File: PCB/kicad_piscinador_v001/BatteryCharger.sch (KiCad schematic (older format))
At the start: 0 parts

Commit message: PCB ----------------- Update
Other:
- note added: "Battery charger"
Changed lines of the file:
@@
 Comment4 ""
 $EndDescr
+Text Notes 3050 1800 0    60   ~ 12
+Battery charger
 $EndSCHEMATC

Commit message: project backup
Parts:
- added BAT?: BATTERY, symbol BATTERY
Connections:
- new net V_gnd: BAT?.2 (-)
- new net V_motor: BAT?.1 (+)
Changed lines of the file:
@@
 LIBS:Zilog
 LIBS:Common-Parts-Library
+LIBS:freetronics_schematic
 LIBS:kicad_test_picinador-cache
 EELAYER 25 0
@@
 Text Notes 3050 1800 0    60   ~ 12
 Battery charger
+$Comp
+L BATTERY BAT?
+U 1 1 57FFC7C9
+P 3400 3000
+F 0 "BAT?" H 3400 3200 50  0000 C CNN
+F 1 "BATTERY" H 3400 2810 50  0000 C CNN
+F 2 "" H 3400 3000 60  0000 C CNN
+F 3 "" H 3400 3000 60  0000 C CNN
+	1    3400 3000
+	0    1    1    0
+$EndComp
+Text HLabel 5000 2700 2    60   Output ~ 0
+V_motor
+Text HLabel 5000 3300 2    60   Output ~ 0
+V_gnd
+Wire Wire Line
+	5000 3300 3400 3300
+Wire Wire Line
+	3400 2700 5000 2700
 $EndSCHEMATC

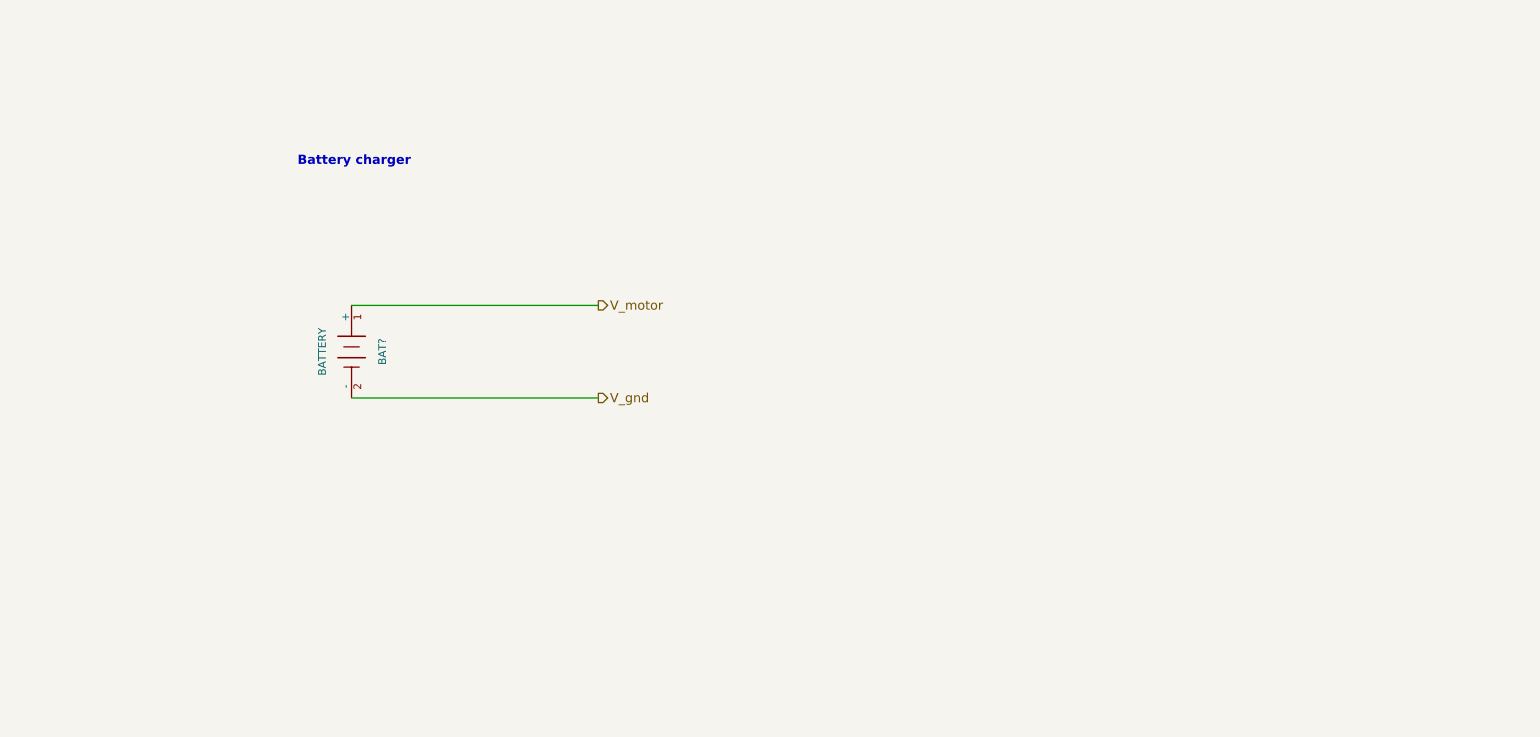
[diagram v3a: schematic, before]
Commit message: Piscinador----------------- Add ltc3121 boost converter
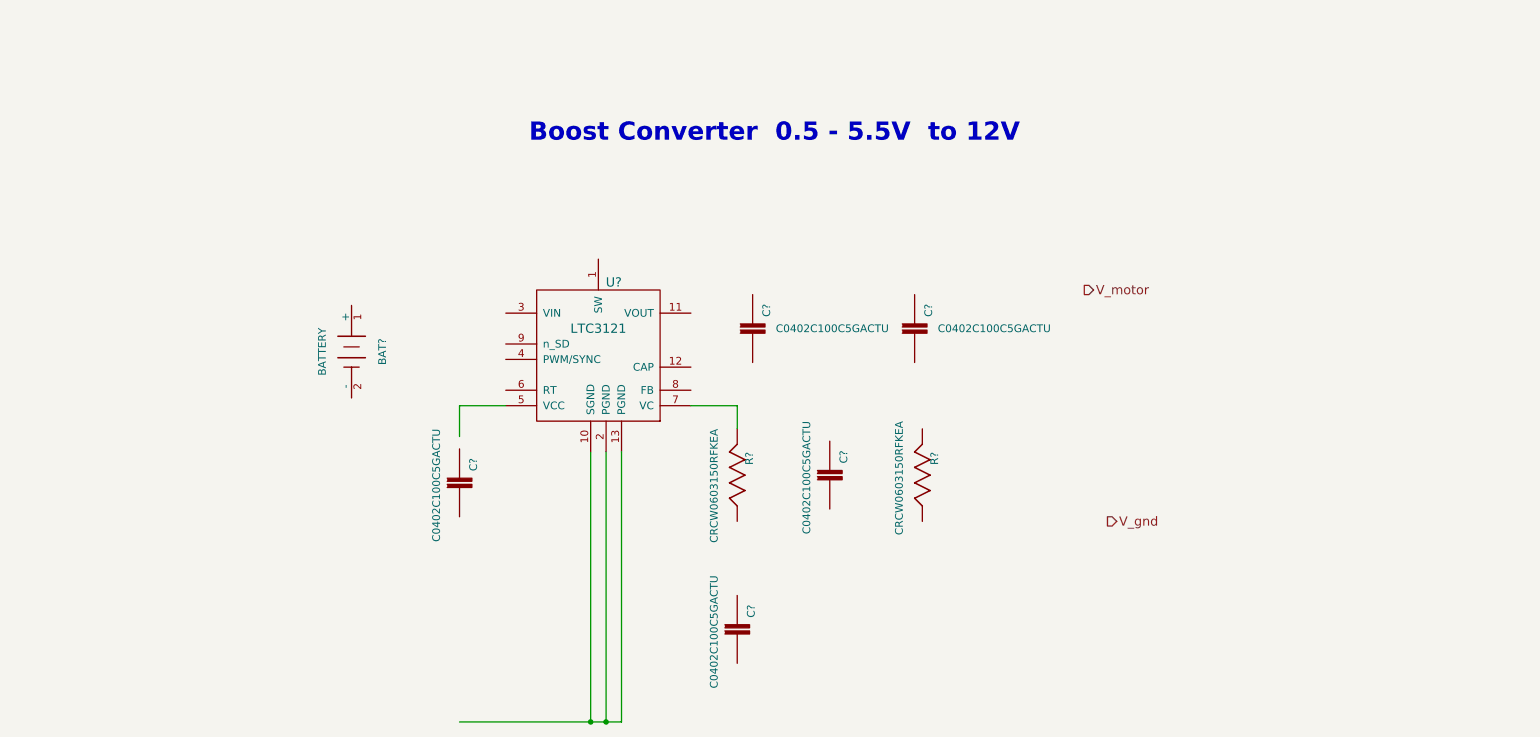
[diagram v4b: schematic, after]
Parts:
- added C? (x5): C0402C100C5GACTU, C0402C100C5GACTU_CAPC1005X60, symbol C0402C100C5GACTU
- added R? (x2): CRCW0603150RFKEA, CRCW0603150RFKEA_RESC1608X55, symbol CRCW0603150RFKEA
- added U?: LTC3121, 12-Lead (4mm × 3mm) Plastic DFN, symbol LTC3121
- BAT?: Manufacturer (none) -> Samsumg
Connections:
- wire segments 2 -> 8
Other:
- note added: "Boost Converter 0.5 - 5.5V to 12V"
- note removed: "Battery charger"
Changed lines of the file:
@@
 LIBS:Zilog
 LIBS:Common-Parts-Library
-LIBS:freetronics_schematic
 LIBS:kicad_test_picinador-cache
 EELAYER 25 0
@@
 encoding utf-8
 Sheet 2 2
-Title "Battery Chager"
-Date ""
+Title "System Spannug "
+Date "2016-10-15"
 Rev ""
-Comp ""
+Comp "JVC-Home"
 Comment1 ""
 Comment2 ""
@@
 Comment4 ""
 $EndDescr
-Text Notes 3050 1800 0    60   ~ 12
-Battery charger
+Text Notes 4550 1650 0    118  ~ 24
+Boost Converter  0.5 - 5.5V  to 12V
 $Comp
 L BATTERY BAT?
@@
 F 2 "" H 3400 3000 60  0000 C CNN
 F 3 "" H 3400 3000 60  0000 C CNN
+F 4 "Samsumg" H 3400 3000 60  0001 C CNN "Manufacturer"
 	1    3400 3000
 	0    1    1    0
 $EndComp
-Text HLabel 5000 2700 2    60   Output ~ 0
+Text HLabel 8150 2600 2    60   Output ~ 0
 V_motor
-Text HLabel 5000 3300 2    60   Output ~ 0
+Text HLabel 8300 4100 2    60   Output ~ 0
 V_gnd
+$Comp
+L LTC3121 U?
+U 1 1 58028389
+P 5050 3150
+F 0 "U?" H 5100 3750 60  0000 C CNN
+F 1 "LTC3121" H 5000 3450 60  0000 C CNN
+F 2 "12-Lead (4mm × 3mm) Plastic DFN" H 5050 3150 60  0001 C CNN
+F 3 "" H 5050 3150 60  0001 C CNN
+F 4 "Linear" H 5050 3150 60  0001 C CNN "Manufaturer"
+F 5 "LTC3121EDE#PBF" H 5050 3150 60  0001 C CNN "Manufacurer No"
+	1    5050 3150
+	1    0    0    -1
+$EndComp
+$Comp
+L C0402C100C5GACTU C?
+U 1 1 580286AA
+P 6000 2850
+F 0 "C?" H 5840 2940 50  0000 L CNN
+F 1 "C0402C100C5GACTU" V 6000 3000 50  0000 L CNN
+F 2 "C0402C100C5GACTU_CAPC1005X60" H 6000 2850 50  0001 L CNN
+F 3 "KEMET" H 6000 2850 50  0001 L CNN
+	1    6000 2850
+	0    1    1    0
+$EndComp
+$Comp
+L CRCW0603150RFKEA R?
+U 1 1 58028919
+P 5900 3800
+F 0 "R?" H 5750 3879 50  0000 L CNN
+F 1 "CRCW0603150RFKEA" H 5600 3650 50  0000 L CNN
+F 2 "CRCW0603150RFKEA_RESC1608X55" H 5900 3800 50  0001 L CNN
+F 3 "VISHAY" H 5900 3800 50  0001 L CNN
+	1    5900 3800
+	0    1    1    0
+$EndComp
+$Comp
+L CRCW0603150RFKEA R?
+U 1 1 58028B0E
+P 7100 3800
+F 0 "R?" H 6950 3879 50  0000 L CNN
+F 1 "CRCW0603150RFKEA" H 6750 3650 50  0000 L CNN
+F 2 "CRCW0603150RFKEA_RESC1608X55" H 7100 3800 50  0001 L CNN
+F 3 "VISHAY" H 7100 3800 50  0001 L CNN
+	1    7100 3800
+	0    1    1    0
+$EndComp
+$Comp
+L C0402C100C5GACTU C?
+U 1 1 58028B45
+P 6500 3800
+F 0 "C?" H 6340 3890 50  0000 L CNN
+F 1 "C0402C100C5GACTU" H 6150 3650 50  0000 L CNN
+F 2 "C0402C100C5GACTU_CAPC1005X60" H 6500 3800 50  0001 L CNN
+F 3 "KEMET" H 6500 3800 50  0001 L CNN
+	1    6500 3800
+	0    1    1    0
+$EndComp
+$Comp
+L C0402C100C5GACTU C?
+U 1 1 58028B7D
+P 7050 2850
+F 0 "C?" H 6890 2940 50  0000 L CNN
+F 1 "C0402C100C5GACTU" V 7050 3000 50  0000 L CNN
+F 2 "C0402C100C5GACTU_CAPC1005X60" H 7050 2850 50  0001 L CNN
+F 3 "KEMET" H 7050 2850 50  0001 L CNN
+	1    7050 2850
+	0    1    1    0
+$EndComp
+$Comp
+L C0402C100C5GACTU C?
+U 1 1 5802911A
+P 4100 3850
+F 0 "C?" H 3940 3940 50  0000 L CNN
+F 1 "C0402C100C5GACTU" H 3750 3700 50  0000 L CNN
+F 2 "C0402C100C5GACTU_CAPC1005X60" H 4100 3850 50  0001 L CNN
+F 3 "KEMET" H 4100 3850 50  0001 L CNN
+	1    4100 3850
+	0    1    1    0
+$EndComp
 Wire Wire Line
-	5000 3300 3400 3300
+	4100 3550 4100 3350
 Wire Wire Line
-	3400 2700 5000 2700
+	4100 3350 4400 3350
+Wire Wire Line
+	4950 3650 4950 5400
+Wire Wire Line
+	5150 5400 4100 5400
+Wire Wire Line
+	5050 3650 5050 5400
+Wire Wire Line
+	5150 3650 5150 5400
+Connection ~ 5050 5400
+Connection ~ 4950 5400
+$Comp
+L C0402C100C5GACTU C?
+U 1 1 5802B8AF
+P 5900 4800
+F 0 "C?" H 5740 4890 50  0000 L CNN
+F 1 "C0402C100C5GACTU" H 5550 4650 50  0000 L CNN
+F 2 "C0402C100C5GACTU_CAPC1005X60" H 5900 4800 50  0001 L CNN
+F 3 "KEMET" H 5900 4800 50  0001 L CNN
+	1    5900 4800
+	0    1    1    0
+$EndComp
+Wire Wire Line
+	5600 3350 5900 3350
+Wire Wire Line
+	5900 3350 5900 3500
 $EndSCHEMATC

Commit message: add plug to charge the battery
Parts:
- removed C? (x5): C0402C100C5GACTU, C0402C100C5GACTU_CAPC1005X60, symbol C0402C100C5GACTU
- added C? (x3): C, symbol C
- added P?: CON_JACK_MONO_SW, symbol CON_JACK_MONO_SW
- added R?: CRCW0603150RFKEA, CRCW0603150RFKEA_RESC1608X55, symbol CRCW0603150RFKEA
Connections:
- wire segments 8 -> 30
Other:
- note added: "Energy harvesting and battery charger"
- moved on the sheet: BAT?, R?, U?
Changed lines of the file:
@@
 LIBS:Zilog
 LIBS:Common-Parts-Library
+LIBS:freetronics_schematic
 LIBS:kicad_test_picinador-cache
 EELAYER 25 0
@@
 Comment4 ""
 $EndDescr
-Text Notes 4550 1650 0    118  ~ 24
+Text Notes 6100 1100 0    118  ~ 24
 Boost Converter  0.5 - 5.5V  to 12V
 $Comp
 L BATTERY BAT?
 U 1 1 57FFC7C9
-P 3400 3000
-F 0 "BAT?" H 3400 3200 50  0000 C CNN
-F 1 "BATTERY" H 3400 2810 50  0000 C CNN
-F 2 "" H 3400 3000 60  0000 C CNN
-F 3 "" H 3400 3000 60  0000 C CNN
-F 4 "Samsumg" H 3400 3000 60  0001 C CNN "Manufacturer"
-	1    3400 3000
+P 6350 3150
+F 0 "BAT?" H 6350 3350 50  0000 C CNN
+F 1 "BATTERY" H 6350 2960 50  0000 C CNN
+F 2 "" H 6350 3150 60  0000 C CNN
+F 3 "" H 6350 3150 60  0000 C CNN
+F 4 "Samsumg" H 6350 3150 60  0001 C CNN "Manufacturer"
+	1    6350 3150
 	0    1    1    0
 $EndComp
-Text HLabel 8150 2600 2    60   Output ~ 0
+Text HLabel 10500 2550 2    60   Output ~ 0
 V_motor
-Text HLabel 8300 4100 2    60   Output ~ 0
+Text HLabel 10600 4650 2    60   Output ~ 0
 V_gnd
 $Comp
 L LTC3121 U?
 U 1 1 58028389
-P 5050 3150
-F 0 "U?" H 5100 3750 60  0000 C CNN
-F 1 "LTC3121" H 5000 3450 60  0000 C CNN
-F 2 "12-Lead (4mm × 3mm) Plastic DFN" H 5050 3150 60  0001 C CNN
-F 3 "" H 5050 3150 60  0001 C CNN
-F 4 "Linear" H 5050 3150 60  0001 C CNN "Manufaturer"
-F 5 "LTC3121EDE#PBF" H 5050 3150 60  0001 C CNN "Manufacurer No"
-	1    5050 3150
+P 8000 3100
+F 0 "U?" H 8050 3700 60  0000 C CNN
+F 1 "LTC3121" H 7950 3400 60  0000 C CNN
+F 2 "12-Lead (4mm × 3mm) Plastic DFN" H 8000 3100 60  0001 C CNN
+F 3 "" H 8000 3100 60  0001 C CNN
+F 4 "Linear" H 8000 3100 60  0001 C CNN "Manufaturer"
+F 5 "LTC3121EDE#PBF" H 8000 3100 60  0001 C CNN "Manufacurer No"
+	1    8000 3100
 	1    0    0    -1
-$EndComp
-$Comp
-L C0402C100C5GACTU C?
-U 1 1 580286AA
-P 6000 2850
-F 0 "C?" H 5840 2940 50  0000 L CNN
-F 1 "C0402C100C5GACTU" V 6000 3000 50  0000 L CNN
-F 2 "C0402C100C5GACTU_CAPC1005X60" H 6000 2850 50  0001 L CNN
-F 3 "KEMET" H 6000 2850 50  0001 L CNN
-	1    6000 2850
-	0    1    1    0
 $EndComp
 $Comp
 L CRCW0603150RFKEA R?
 U 1 1 58028919
-P 5900 3800
-F 0 "R?" H 5750 3879 50  0000 L CNN
-F 1 "CRCW0603150RFKEA" H 5600 3650 50  0000 L CNN
-F 2 "CRCW0603150RFKEA_RESC1608X55" H 5900 3800 50  0001 L CNN
-F 3 "VISHAY" H 5900 3800 50  0001 L CNN
-	1    5900 3800
+P 8850 3750
+F 0 "R?" H 8700 3829 50  0000 L CNN
+F 1 "CRCW0603150RFKEA" H 8550 3600 50  0000 L CNN
+F 2 "CRCW0603150RFKEA_RESC1608X55" H 8850 3750 50  0001 L CNN
+F 3 "VISHAY" H 8850 3750 50  0001 L CNN
+	1    8850 3750
 	0    1    1    0
 $EndComp
@@
 L CRCW0603150RFKEA R?
 U 1 1 58028B0E
-P 7100 3800
-F 0 "R?" H 6950 3879 50  0000 L CNN
-F 1 "CRCW0603150RFKEA" H 6750 3650 50  0000 L CNN
-F 2 "CRCW0603150RFKEA_RESC1608X55" H 7100 3800 50  0001 L CNN
-F 3 "VISHAY" H 7100 3800 50  0001 L CNN
-	1    7100 3800
-	0    1    1    0
-$EndComp
-$Comp
-L C0402C100C5GACTU C?
-U 1 1 58028B45
-P 6500 3800
-F 0 "C?" H 6340 3890 50  0000 L CNN
-F 1 "C0402C100C5GACTU" H 6150 3650 50  0000 L CNN
-F 2 "C0402C100C5GACTU_CAPC1005X60" H 6500 3800 50  0001 L CNN
-F 3 "KEMET" H 6500 3800 50  0001 L CNN
-	1    6500 3800
-	0    1    1    0
-$EndComp
-$Comp
-L C0402C100C5GACTU C?
-U 1 1 58028B7D
-P 7050 2850
-F 0 "C?" H 6890 2940 50  0000 L CNN
-F 1 "C0402C100C5GACTU" V 7050 3000 50  0000 L CNN
-F 2 "C0402C100C5GACTU_CAPC1005X60" H 7050 2850 50  0001 L CNN
-F 3 "KEMET" H 7050 2850 50  0001 L CNN
-	1    7050 2850
-	0    1    1    0
-$EndComp
-$Comp
-L C0402C100C5GACTU C?
-U 1 1 5802911A
-P 4100 3850
-F 0 "C?" H 3940 3940 50  0000 L CNN
-F 1 "C0402C100C5GACTU" H 3750 3700 50  0000 L CNN
-F 2 "C0402C100C5GACTU_CAPC1005X60" H 4100 3850 50  0001 L CNN
-F 3 "KEMET" H 4100 3850 50  0001 L CNN
-	1    4100 3850
+P 9350 3750
+F 0 "R?" H 9200 3829 50  0000 L CNN
+F 1 "CRCW0603150RFKEA" H 9000 3600 50  0000 L CNN
+F 2 "CRCW0603150RFKEA_RESC1608X55" H 9350 3750 50  0001 L CNN
+F 3 "VISHAY" H 9350 3750 50  0001 L CNN
+	1    9350 3750
 	0    1    1    0
 $EndComp
 Wire Wire Line
-	4100 3550 4100 3350
+	7200 3300 7200 3650
 Wire Wire Line
-	4100 3350 4400 3350
+	7200 3300 7500 3300
 Wire Wire Line
-	4950 3650 4950 5400
+	7900 3600 7900 4650
 Wire Wire Line
-	5150 5400 4100 5400
+	5600 4650 6350 4650
 Wire Wire Line
-	5050 3650 5050 5400
+	6350 4650 7200 4650
 Wire Wire Line
-	5150 3650 5150 5400
-Connection ~ 5050 5400
-Connection ~ 4950 5400
+	7200 4650 7900 4650
+Wire Wire Line
+	7900 4650 8000 4650
+Wire Wire Line
+	8000 4650 8100 4650
+Wire Wire Line
+	8100 4650 8850 4650
+Wire Wire Line
+	8850 4650 9350 4650
+Wire Wire Line
+	9350 4650 10750 4650
+Wire Wire Line
+	8000 3600 8000 4650
+Wire Wire Line
+	8100 3600 8100 4650
+Connection ~ 8000 4650
+Connection ~ 7900 4650
+Wire Wire Line
+	8550 3300 8850 3300
+Wire Wire Line
+	8850 3300 8850 3450
+Connection ~ 8100 4650
+Wire Wire Line
+	8550 2700 8550 2550
+Wire Wire Line
+	9350 2550 10500 2550
+Wire Wire Line
+	8550 3050 9000 3050
+Wire Wire Line
+	8550 3200 9350 3200
+Wire Wire Line
+	9350 3200 9350 3450
 $Comp
-L C0402C100C5GACTU C?
-U 1 1 5802B8AF
-P 5900 4800
-F 0 "C?" H 5740 4890 50  0000 L CNN
-F 1 "C0402C100C5GACTU" H 5550 4650 50  0000 L CNN
-F 2 "C0402C100C5GACTU_CAPC1005X60" H 5900 4800 50  0001 L CNN
-F 3 "KEMET" H 5900 4800 50  0001 L CNN
-	1    5900 4800
+L C C?
+U 1 1 5803755E
+P 8750 2800
+F 0 "C?" H 8775 2900 50  0000 L CNN
+F 1 "C" H 8775 2700 50  0000 L CNN
+F 2 "" H 8788 2650 50  0000 C CNN
+F 3 "" H 8750 2800 50  0000 C CNN
+	1    8750 2800
+	1    0    0    -1
+$EndComp
+$Comp
+L C C?
+U 1 1 5803780A
+P 8850 4300
+F 0 "C?" H 8875 4400 50  0000 L CNN
+F 1 "C" H 8875 4200 50  0000 L CNN
+F 2 "" H 8888 4150 50  0000 C CNN
+F 3 "" H 8850 4300 50  0000 C CNN
+	1    8850 4300
+	1    0    0    -1
+$EndComp
+$Comp
+L C C?
+U 1 1 58037850
+P 7200 3800
+F 0 "C?" H 7225 3900 50  0000 L CNN
+F 1 "C" H 7225 3700 50  0000 L CNN
+F 2 "" H 7238 3650 50  0000 C CNN
+F 3 "" H 7200 3800 50  0000 C CNN
+	1    7200 3800
+	1    0    0    -1
+$EndComp
+Wire Wire Line
+	8850 4050 8850 4150
+Wire Wire Line
+	9350 4050 9350 4650
+Connection ~ 9350 4650
+Wire Wire Line
+	8850 4450 8850 4650
+Connection ~ 8850 4650
+Wire Wire Line
+	7200 3950 7200 4650
+$Comp
+L CRCW0603150RFKEA R?
+U 1 1 58037C47
+P 9350 2900
+F 0 "R?" H 9200 2979 50  0000 L CNN
+F 1 "CRCW0603150RFKEA" H 9000 2750 50  0000 L CNN
+F 2 "CRCW0603150RFKEA_RESC1608X55" H 9350 2900 50  0001 L CNN
+F 3 "VISHAY" H 9350 2900 50  0001 L CNN
+	1    9350 2900
 	0    1    1    0
 $EndComp
 Wire Wire Line
-	5600 3350 5900 3350
+	9350 2600 9350 2550
+Wire Notes Line
+	6950 5150 6950 5150
+$Comp
+L CON_JACK_MONO_SW P?
+U 1 1 58037EB1
+P 5100 2800
+F 0 "P?" H 4750 3050 60  0000 C CNN
+F 1 "CON_JACK_MONO_SW" H 5150 2600 60  0000 C CNN
+F 2 "" H 5100 2800 60  0000 C CNN
+F 3 "" H 5100 2800 60  0000 C CNN
+	1    5100 2800
+	1    0    0    1
+$EndComp
 Wire Wire Line
-	5900 3350 5900 3500
+	5600 2700 7350 2700
+Connection ~ 7200 4650
+Wire Wire Line
+	5600 2950 5600 4650
+Connection ~ 6350 4650
+Wire Wire Line
+	5600 2800 6350 2800
+Wire Wire Line
+	6350 2800 6350 2850
+Wire Wire Line
+	6350 3450 6350 4650
+Text Notes 1200 1000 0    118  ~ 24
+Energy harvesting and battery charger
 $EndSCHEMATC
